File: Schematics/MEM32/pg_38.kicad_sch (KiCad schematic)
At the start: 34 parts, among them U3901 1MEG, U3902 1MEG, U3903 1MEG, U3904 1MEG, U3905 1MEG, U3906 1MEG, U3907 1MEG, U3908 1MEG, U3909 1MEG, U3910 1MEG, U3911 1MEG, U3912 1MEG, U3913 1MEG, U3914 1MEG, U3915 1MEG, U3916 1MEG, U3917 1MEG, U3918 1MEG, U3919 1MEG, U3920 1MEG, U3921 1MEG, U3922 1MEG, U3923 1MEG, U3924 1MEG, U3925 1MEG, U3926 1MEG, U3927 1MEG, U3928 1MEG, U3929 1MEG, U3930 1MEG, U3931 1MEG, U3932 1MEG, U3933 1MEG, U3934 1MEG

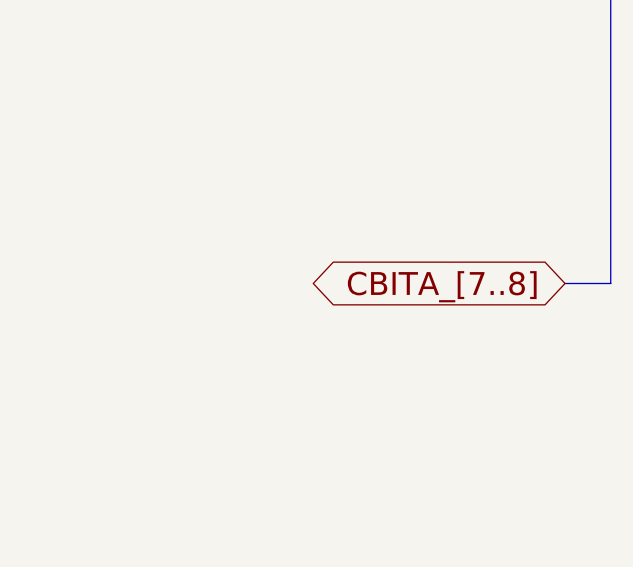
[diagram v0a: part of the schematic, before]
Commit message: More typos
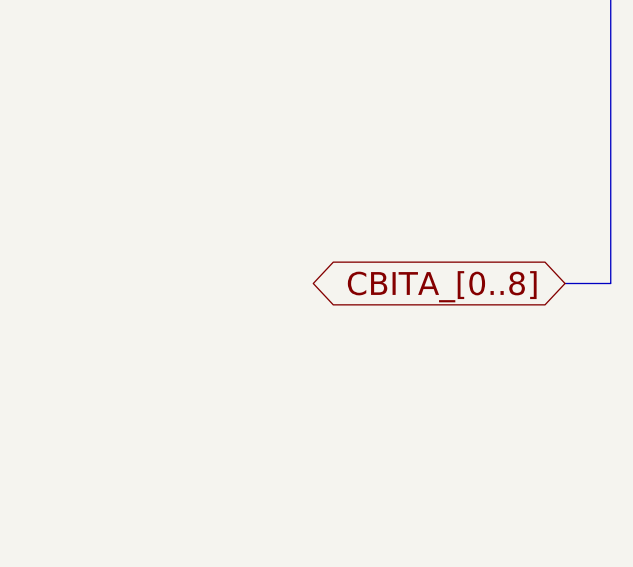
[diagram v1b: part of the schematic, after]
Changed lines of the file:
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@@
   (junction (at 553.72 55.88) (diameter 0) (color 0 0 0 0) )
   (junction (at 553.72 124.46) (diameter 0) (color 0 0 0 0) )
-  (global_label "CBITA_[7..8]" (shape bidirectional) (at 563.88 246.38 180) (fields_autoplaced) (effects (font (size 2.54 2.54) ) (justify right) ) (property "Intersheet References" "${INTERSHEET_REFS}" (id 0) (at 536.073 246.2213 0) (effects (font (size 2.54 2.54) ) (justify right) ) ) )
+  (global_label "CBITA_[0..8]" (shape bidirectional) (at 563.88 246.38 180) (fields_autoplaced) (effects (font (size 2.54 2.54) ) (justify right) ) (property "Intersheet References" "${INTERSHEET_REFS}" (id 0) (at 536.073 246.2213 0) (effects (font (size 2.54 2.54) ) (justify right) ) ) )
   (bus_entry (at 568.96 53.34) (size -2.54 2.54) )
   (bus_entry (at 568.96 121.92) (size -2.54 2.54) )

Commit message: TYP/VAL busses
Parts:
- removed U3901, U3902, U3903, U3904, U3905, U3906, U3907, U3908, U3909, U3910, U3911, U3912, U3913, U3914, U3915, U3916, U3917, U3918, U3919, U3920, U3921, U3922, U3923, U3924, U3925, U3926, U3927, U3928, U3929, U3930, U3931, U3932, U3933, U3934: 1MEG, symbol r1000:1MEG
- added U (x2): (no value), symbol r1000:1MEG
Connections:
- net AAA1: now also U.15 (A1), U.15 (A1)
- net AAA10: now also U.5 (A10), U.5 (A10)
- net AAA2: now also U.14 (A2), U.14 (A2)
- net AAA3: now also U.13 (A3), U.13 (A3)
- net AAA4: now also U.12 (A4), U.12 (A4)
- net AAA5: now also U.11 (A5), U.11 (A5)
- net AAA6: now also U.10 (A6), U.10 (A6)
- net AAA7: now also U.8 (A7), U.8 (A7)
- net AAA8: now also U.7 (A8), U.7 (A8)
- net AAA9: now also U.6 (A9), U.6 (A9)
- net AACAS~: now also U.16 (CAS), U.16 (CAS)
- net AARAS~: now also U.3 (RAS), U.3 (RAS)
- net AAWE~: now also U.2 (WE), U.2 (WE)
- net CBITA_7: now also U.1 (D), U.17 (Q)
- net CBITA_8: now also U.1 (D), U.17 (Q)

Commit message: MEM32 tested to 6.12s (rm022)
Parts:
- removed U (x2): (no value), symbol r1000:1MEG
